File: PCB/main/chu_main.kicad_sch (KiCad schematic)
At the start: 111 parts, among them K1 Conn_01x01_Female, K10 Conn_01x01_Female, K11 Conn_01x01_Female, K12 Conn_01x01_Female, K13 Conn_01x01_Female, K14 Conn_01x01_Female, K15 Conn_01x01_Female, K16 Conn_01x01_Female, K17 Conn_01x01_Female, K18 Conn_01x01_Female, K19 Conn_01x01_Female, K2 Conn_01x01_Female, K20 Conn_01x01_Female, K21 Conn_01x01_Female, K22 Conn_01x01_Female, K23 Conn_01x01_Female, K24 Conn_01x01_Female, K25 Conn_01x01_Female, K26 Conn_01x01_Female, K27 Conn_01x01_Female, K28 Conn_01x01_Female, K29 Conn_01x01_Female, K3 Conn_01x01_Female, K30 Conn_01x01_Female, K31 Conn_01x01_Female, K32 Conn_01x01_Female, K4 Conn_01x01_Female, K5 Conn_01x01_Female, K6 Conn_01x01_Female, K7 Conn_01x01_Female, K8 Conn_01x01_Female, K9 Conn_01x01_Female, U0 ChuAcrylic, U1 Pico, U2 PCA9548APW, U3 MPR121QR2_BOARD, U4 MPR121QR2_BOARD, U5 MPR121QR2_BOARD, U8 SN74LV1T34DBV, X1 GP2Y0E03_REAL, X2 GP2Y0E03_REAL, X3 GP2Y0E03_REAL, X4 GP2Y0E03_REAL, X5 GP2Y0E03_REAL

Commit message: PCB v1.4 (reduce crosstalk)
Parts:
- K11, K14, K23, K26: footprint chu_main:ChuKey -> chu_main:ChuKeyBiasLeft
- K12, K13, K24, K25: footprint chu_main:ChuKey -> chu_main:ChuKeyBiasRight
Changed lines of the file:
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@@
       (effects (font (size 1.27 1.27)) (justify left) hide)
     )
-    (property "Footprint" "chu_main:ChuKey" (id 2) (at 354.33 55.88 0)
+    (property "Footprint" "chu_main:ChuKeyBiasLeft" (id 2) (at 354.33 55.88 0)
       (effects (font (size 1.27 1.27)) hide)
     )
@@
       (effects (font (size 1.27 1.27)) (justify left) hide)
     )
-    (property "Footprint" "chu_main:ChuKey" (id 2) (at 354.33 90.17 0)
+    (property "Footprint" "chu_main:ChuKeyBiasLeft" (id 2) (at 354.33 90.17 0)
       (effects (font (size 1.27 1.27)) hide)
     )
@@
       (effects (font (size 1.27 1.27)) (justify left) hide)
     )
-    (property "Footprint" "chu_main:ChuKey" (id 2) (at 354.33 113.03 0)
+    (property "Footprint" "chu_main:ChuKeyBiasLeft" (id 2) (at 354.33 113.03 0)
       (effects (font (size 1.27 1.27)) hide)
     )
@@
       (effects (font (size 1.27 1.27)) (justify left) hide)
     )
-    (property "Footprint" "chu_main:ChuKey" (id 2) (at 354.33 144.78 0)
+    (property "Footprint" "chu_main:ChuKeyBiasRight" (id 2) (at 354.33 144.78 0)
       (effects (font (size 1.27 1.27)) hide)
     )
@@
       (effects (font (size 1.27 1.27)) (justify left) hide)
     )
-    (property "Footprint" "chu_main:ChuKey" (id 2) (at 354.33 115.57 0)
+    (property "Footprint" "chu_main:ChuKeyBiasRight" (id 2) (at 354.33 115.57 0)
       (effects (font (size 1.27 1.27)) hide)
     )
@@
       (effects (font (size 1.27 1.27)) (justify left) hide)
     )
-    (property "Footprint" "chu_main:ChuKey" (id 2) (at 354.33 147.32 0)
+    (property "Footprint" "chu_main:ChuKeyBiasLeft" (id 2) (at 354.33 147.32 0)
       (effects (font (size 1.27 1.27)) hide)
     )
@@
       (effects (font (size 1.27 1.27)) (justify left) hide)
     )
-    (property "Footprint" "chu_main:ChuKey" (id 2) (at 354.33 58.42 0)
+    (property "Footprint" "chu_main:ChuKeyBiasRight" (id 2) (at 354.33 58.42 0)
       (effects (font (size 1.27 1.27)) hide)
     )
@@
       (effects (font (size 1.27 1.27)) (justify left) hide)
     )
-    (property "Footprint" "chu_main:ChuKey" (id 2) (at 354.33 87.63 0)
+    (property "Footprint" "chu_main:ChuKeyBiasRight" (id 2) (at 354.33 87.63 0)
       (effects (font (size 1.27 1.27)) hide)
     )
@@
     )
     (path "/0563fcc7-e713-4f2d-9e87-2634364fb680"
-      (reference "K11") (unit 1) (value "Conn_01x01_Female") (footprint "chu_main:ChuKey")
+      (reference "K11") (unit 1) (value "Conn_01x01_Female") (footprint "chu_main:ChuKeyBiasLeft")
     )
     (path "/db4705d9-b3d2-49a4-96f3-33f3ee5db3c5"
-      (reference "K12") (unit 1) (value "Conn_01x01_Female") (footprint "chu_main:ChuKey")
+      (reference "K12") (unit 1) (value "Conn_01x01_Female") (footprint "chu_main:ChuKeyBiasRight")
     )
     (path "/fdd4bd59-1d65-42a6-b5bf-d786dc261db6"
-      (reference "K13") (unit 1) (value "Conn_01x01_Female") (footprint "chu_main:ChuKey")
+      (reference "K13") (unit 1) (value "Conn_01x01_Female") (footprint "chu_main:ChuKeyBiasRight")
     )
     (path "/1cc33a48-faf2-4585-867a-a271a201d1c5"
-      (reference "K14") (unit 1) (value "Conn_01x01_Female") (footprint "chu_main:ChuKey")
+      (reference "K14") (unit 1) (value "Conn_01x01_Female") (footprint "chu_main:ChuKeyBiasLeft")
     )
     (path "/551e7bff-6472-460c-adbb-2baecd766975"
@@
     )
     (path "/70b72b6d-13c0-49b6-9606-488d841a2a1e"
-      (reference "K23") (unit 1) (value "Conn_01x01_Female") (footprint "chu_main:ChuKey")
+      (reference "K23") (unit 1) (value "Conn_01x01_Female") (footprint "chu_main:ChuKeyBiasLeft")
     )
     (path "/ae98f63d-97f8-4350-916b-711df88aa422"
-      (reference "K24") (unit 1) (value "Conn_01x01_Female") (footprint "chu_main:ChuKey")
+      (reference "K24") (unit 1) (value "Conn_01x01_Female") (footprint "chu_main:ChuKeyBiasRight")
     )
     (path "/9dffab08-f394-41c2-8837-8cc9e3f1bf44"
-      (reference "K25") (unit 1) (value "Conn_01x01_Female") (footprint "chu_main:ChuKey")
+      (reference "K25") (unit 1) (value "Conn_01x01_Female") (footprint "chu_main:ChuKeyBiasRight")
     )
     (path "/bed81a25-aad1-400c-b41d-73f476c42ab9"
-      (reference "K26") (unit 1) (value "Conn_01x01_Female") (footprint "chu_main:ChuKey")
+      (reference "K26") (unit 1) (value "Conn_01x01_Female") (footprint "chu_main:ChuKeyBiasLeft")
     )
     (path "/40517cf5-e968-448a-8be5-e06b125a310d"

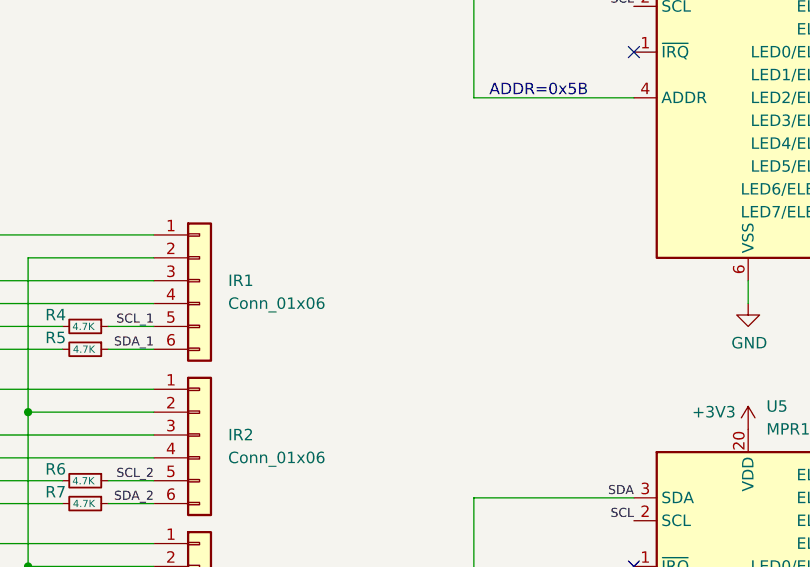
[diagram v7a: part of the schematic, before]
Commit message: PCB v1.5 for dedicate PN532 pads
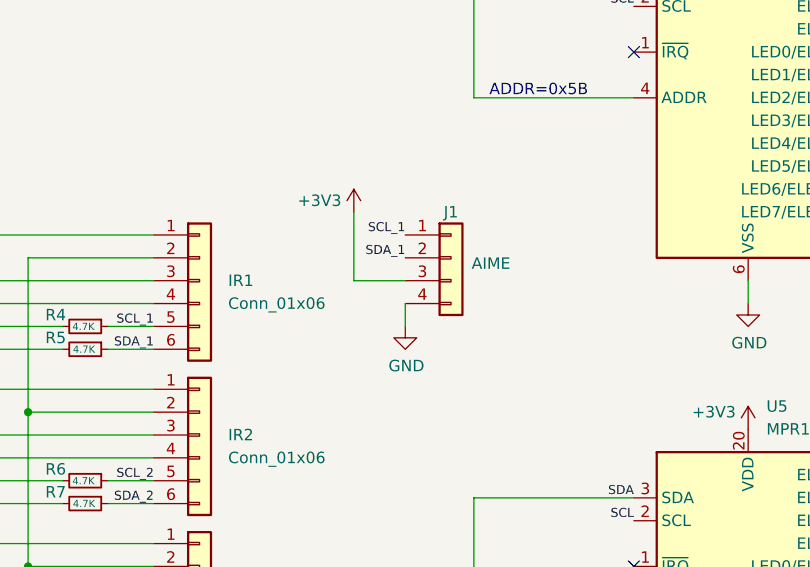
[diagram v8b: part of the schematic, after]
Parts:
- added J1: Conn_01x04, chu_main:PN532, symbol Connector_Generic:Conn_01x04
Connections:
- net +3V3: now also J1.3 (Pin_3)
- net GND: now also J1.4 (Pin_4)
- net SCL_1: now also J1.1 (Pin_1)
- net SDA_1: now also J1.2 (Pin_2)
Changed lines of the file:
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@@
     (stroke (width 0) (type default) (color 0 0 0 0))
   )
+  (wire (pts (xy 283.845 123.19) (xy 283.845 115.57))
+    (stroke (width 0) (type default) (color 0 0 0 0))
+  )
   (wire (pts (xy 327.66 68.58) (xy 327.66 66.04))
     (stroke (width 0) (type default) (color 0 0 0 0))
@@
     (stroke (width 0) (type default) (color 0 0 0 0))
   )
+  (wire (pts (xy 289.56 123.19) (xy 283.845 123.19))
+    (stroke (width 0) (type default) (color 0 0 0 0))
+  )
   (wire (pts (xy 176.53 180.34) (xy 179.705 180.34))
     (stroke (width 0) (type default) (color 0 0 0 0))
@@
     (stroke (width 0) (type default) (color 0 0 0 0))
   )
+  (wire (pts (xy 289.56 125.73) (xy 289.56 128.27))
+    (stroke (width 0) (type default) (color 0 0 0 0))
+  )
   (wire (pts (xy 181.61 76.2) (xy 186.69 76.2))
     (stroke (width 0) (type default) (color 0 0 0 0))
@@
     (effects (font (size 1 1)) (justify left bottom))
   )
+  (label "SDA_1" (at 289.56 120.65 180)
+    (effects (font (size 1 1)) (justify right bottom))
+  )
   (label "SCL_4" (at 261.62 179.705 180)
     (effects (font (size 1 1)) (justify right bottom))
@@
     (effects (font (size 1 1)) (justify left bottom))
   )
+  (label "SCL_1" (at 289.56 118.11 180)
+    (effects (font (size 1 1)) (justify right bottom))
+  )
   (label "SDA_3" (at 200.025 154.94 0)
     (effects (font (size 1 1)) (justify left bottom))
@@
     (pin "1")
   )
+  (symbol (lib_id "power:GND") (at 289.56 128.27 0) (unit 1)
+    (in_bom yes) (on_board yes)
+    (property "Reference" "#PWR?" (id 0) (at 289.56 134.62 0)
+      (effects (font (size 1.27 1.27)) hide)
+    )
+    (property "Value" "GND" (id 1) (at 289.687 132.6642 0))
+    (property "Footprint" "" (id 2) (at 289.56 128.27 0)
+      (effects (font (size 1.27 1.27)) hide)
+    )
+    (property "Datasheet" "" (id 3) (at 289.56 128.27 0)
+      (effects (font (size 1.27 1.27)) hide)
+    )
+    (pin "1")
+  )
   (symbol (lib_id "Device:R_Small") (at 254 145.415 270) (unit 1)
     (in_bom yes) (on_board yes)
@@
     (pin "2")
   )
+  (symbol (lib_id "power:+3V3") (at 283.845 115.57 0) (unit 1)
+    (in_bom yes) (on_board yes)
+    (property "Reference" "#PWR?" (id 0) (at 283.845 119.38 0)
+      (effects (font (size 1.27 1.27)) hide)
+    )
+    (property "Value" "+3V3" (id 1) (at 280.035 114.3 0))
+    (property "Footprint" "" (id 2) (at 283.845 115.57 0)
+      (effects (font (size 1.27 1.27)) hide)
+    )
+    (property "Datasheet" "" (id 3) (at 283.845 115.57 0)
+      (effects (font (size 1.27 1.27)) hide)
+    )
+    (pin "1")
+  )
   (symbol (lib_id "Connector:Conn_01x01_Female") (at 354.33 95.25 0) (unit 1)
     (in_bom yes) (on_board yes)
@@
     (pin "2")
   )
+  (symbol (lib_id "Connector_Generic:Conn_01x04") (at 294.64 120.65 0) (unit 1)
+    (in_bom yes) (on_board yes)
+    (property "Reference" "J1" (id 0) (at 294.64 115.57 0))
+    (property "Value" "Conn_01x04" (id 1) (at 294.64 130.175 0)
+      (effects (font (size 1.27 1.27)) hide)
+    )
+    (property "Footprint" "chu_main:PN532" (id 2) (at 294.64 120.65 0)
+      (effects (font (size 1.27 1.27)) hide)
+    )
+    (property "Datasheet" "" (id 3) (at 294.64 120.65 0)
+      (effects (font (size 1.27 1.27)) hide)
+    )
+    (property "Field4" "AIME" (id 4) (at 299.085 121.285 0))
+    (pin "1")
+    (pin "2")
+    (pin "3")
+    (pin "4")
+  )
   (symbol (lib_id "chu_main:WS2812B_Unified") (at 133.35 217.17 0) (unit 1)
     (in_bom yes) (on_board yes)
@@
       (reference "#PWR0126") (unit 1) (value "GND") (footprint "")
     )
+    (path "/6222c6db-4864-48d1-bb14-18d53d5ada32"
+      (reference "#PWR?") (unit 1) (value "GND") (footprint "")
+    )
+    (path "/a2de4610-6397-4073-a455-d28e2cff2a2a"
+      (reference "#PWR?") (unit 1) (value "+3V3") (footprint "")
+    )
     (path "/9494815a-0a19-4608-bd5d-ef347ed4e840"
       (reference "C1") (unit 1) (value "0.1uF") (footprint "Capacitor_SMD:C_0603_1608Metric_Pad1.08x0.95mm_HandSolder")
@@
       (reference "IR5") (unit 1) (value "Conn_01x06") (footprint "chu_main:GP2Y0E03")
     )
+    (path "/f05750a0-de1e-4872-872a-38fb56289bbe"
+      (reference "J1") (unit 1) (value "Conn_01x04") (footprint "chu_main:PN532")
+    )
     (path "/23b2cb74-c5fc-4a0c-90a7-9aa067f7224d"
